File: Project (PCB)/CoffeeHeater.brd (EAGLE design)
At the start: 231.1 x 182.6 mm, 9 parts, among them U1 POCKETBEAGLE, U2 0.56_HEX_BACKPACK

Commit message: Updated the library with all the devices and made progress in the schematics and the board
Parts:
- removed D2, D3: LED, ENGI301:EIA-STD
- added BLUE, GREEN, RED: LED, ENGI301:EIA-STD
- added C1, C2: 10uF/16V X5R, microbuilder:0805-NO
- added C3: 0.1uF, microbuilder:0805-NO
- added C4: 10pF, microbuilder:0805-NO
- added C5, C6, C7: 22uF/10V X5R, microbuilder:0805-NO
- added C8: 1uF/10V X5R, microbuilder:0805-NO
- added L1: NRS5030T1R0NMGJ, microbuilder:INDUCTOR_5X5MM_TDK_VLC5045
- added Q1: BSS138, microbuilder:SOT23-WIDE
- added R10, R6, R9: 105K, microbuilder:0805-NO
- added R4: 2.2k, ENGI301:R0603
- added R5, R7: 1M, microbuilder:0805-NO
- added R8: 1K, microbuilder:0805-NO
- added U$2: TIP32C_TRANSISTOR, CoffeeHeater:TIP32C_TRANSISTOR
- added U$3: DIODE, CoffeeHeater:DIODE
- added U$4: HEATING_PAD, CoffeeHeater:HEATING_PAD
- added U3: TPS63060, microbuilder:PWSON-N10
- added X1: (no value), microbuilder:TERMBLOCK_1X2-3.5MM
- D1: value LED -> GREEN; device ENGI301:EIA-STD -> microbuilder:CHIPLED_0805_NOOUTLINE
- moved U$1 190.5 mm to (77.5, 78.7)
- moved D1 181.6 mm to (143.5, 85.1)
- moved R1 149.9 mm to (80.0, 40.6)
- moved R3 102.4 mm to (27.9, 52.1)
- moved R2 101.2 mm to (27.9, 45.7)
- moved U1 96.8 mm to (9.40, 58.7)
- moved U2 78.8 mm to (35.6, 24.1)
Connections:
- removed net VIN: U1.1
- new net 12V_VIN: C1.1, C2.1, R9.1, U$2.C, U3.2, X1.2
- new net 5.0V: C5.1, C6.1, C7.1, C8.1, D1.A, R5.2, R7.2, U1.1, U3.9
- new net BASE: U$2.B, U$3.OUT
- new net ENABLE: R9.2, U3.3
- new net HEAT_CONTROL: U$3.IN, U1.60
- new net N$1: U$2.E, U$4.GND
- new net N$10: D1.C, R8.1
- new net N$11: Q1.3, R8.2
- new net N$6: L1.P$1, U3.1
- new net N$7: L1.P$2, U3.10
- new net N$8: C3.1, U3.6
- new net N$9: C4.1, R5.1, R6.2, U3.8
- new net PG: Q1.1, R7.1, U3.5
- new net PS: R10.1, U3.4
- new net TEMP: R4.2, U$1.DQ, U1.69
- net GND: now also BLUE.P$2, C1.2, C2.2, C3.2, C4.2, C5.2, C6.2, C7.2, C8.2, GREEN.P$2, Q1.2, R10.2, R6.1, RED.P$2, U$1.GND, U$4.VDD, U3.7, U3.THERMAL@1, U3.THERMAL@10, U3.THERMAL@11, U3.THERMAL@12, U3.THERMAL@13, U3.THERMAL@14, U3.THERMAL@5, U3.THERMAL@6, U3.THERMAL@7, U3.THERMAL@8, U3.THERMAL@9, X1.1; no longer D1.P$2, D2.P$2, D3.P$2
- net N$3: now also U1.71; no longer U1.19
- net START_0: now also BLUE.P$1, U1.54; no longer D1.P$1, U1.55
- net START_1: now also GREEN.P$1, U1.56; no longer D2.P$1, U1.60
- net START_2: now also RED.P$1; no longer D3.P$1
- net VDD_5V: now also R4.1, U$1.VDD
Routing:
- added copper zone on layer 16, net GND
- added copper zone on layer 1, net VDD_3P3V
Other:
- board size 231.1 x 182.6 mm -> 152.4 x 101.6 mm
- board text added: "HEATING_PAD"
- board text added: "TIP32C_Potentiometer"

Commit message: Started routing some of the connections
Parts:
- moved R2 17.0 mm to (45.0, 45.5)
- moved R3 17.0 mm to (45.0, 51.8)
- moved R4 0.25 mm to (70.1, 87.6), turned to 180 degrees
- flipped BLUE to the bottom
- flipped GREEN to the bottom
- flipped R1 to the bottom
- flipped RED to the bottom
- flipped U2 to the bottom
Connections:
- net GND: now also U$4.GND; no longer U$4.VDD
- net N$1: now also U$4.VDD; no longer U$4.GND
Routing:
- net START_0: track 0.00 -> 104.9 mm
- net VDD_5V: track 0.00 -> 98.5 mm
- net HEAT_CONTROL: track 0.00 -> 96.7 mm
- net START_1: track 0.00 -> 92.6 mm
- net START_2: track 0.00 -> 81.9 mm
- net N$2: track 0.00 -> 75.1 mm
- net N$3: track 0.00 -> 63.6 mm
- net TEMP: track 0.00 -> 41.5 mm
- net I2C_SDA: track 0.00 -> 33.2 mm
- net I2C_SCL: track 0.00 -> 33.0 mm
- net N$1: track 0.00 -> 20.8 mm
- net BASE: track 0.00 -> 12.7 mm

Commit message: Connect all the GND nets
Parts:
- moved R8 0.80 mm to (143.5, 73.7), turned to 270 degrees
- moved D1 0.25 mm to (143.5, 84.8), turned to 180 degrees
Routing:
- net GND: track 0.00 -> 53.5 mm, vias 0 -> 18
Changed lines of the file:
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@@
 <attribute name="NAME" x="134.747" y="83.312" size="0.8128" layer="25" ratio="18" rot="R90"/>
 </element>
-<element name="D1" library="microbuilder" package="CHIPLED_0805_NOOUTLINE" value="GREEN" x="143.51" y="85.09">
-<attribute name="NAME" x="142.494" y="83.312" size="0.8128" layer="25" ratio="18" rot="R90"/>
-<attribute name="VALUE" x="144.907" y="83.566" size="0.4064" layer="27" ratio="10" rot="R90"/>
-</element>
-<element name="R8" library="microbuilder" package="0805-NO" value="1K" x="143.764" y="72.898" rot="R90">
-<attribute name="NAME" x="142.621" y="71.12" size="0.8128" layer="25" ratio="18" rot="R90"/>
+<element name="D1" library="microbuilder" package="CHIPLED_0805_NOOUTLINE" value="GREEN" x="143.51" y="84.836" rot="R180">
+<attribute name="NAME" x="141.478" y="84.328" size="0.8128" layer="25" ratio="18" rot="R270"/>
+<attribute name="VALUE" x="144.907" y="84.836" size="0.4064" layer="27" ratio="10" rot="R270"/>
+</element>
+<element name="R8" library="microbuilder" package="0805-NO" value="1K" x="143.51" y="73.66" rot="R270">
+<attribute name="NAME" x="144.653" y="75.438" size="0.8128" layer="25" ratio="18" rot="R270"/>
 </element>
 <element name="X1" library="microbuilder" package="TERMBLOCK_1X2-3.5MM" value="" x="86.106" y="66.167" rot="R90">
@@
 </polygon>
 <contactref element="U$4" pad="GND"/>
-<wire x1="129.54" y1="86.04" x2="135.89" y2="86.04" width="0" layer="19" extent="1-1"/>
-<wire x1="123.19" y1="86.04" x2="129.54" y2="86.04" width="0" layer="19" extent="1-1"/>
-<wire x1="116.84" y1="86.04" x2="123.19" y2="86.04" width="0" layer="19" extent="1-1"/>
-<wire x1="130.318" y1="72.71" x2="129.54" y2="86.04" width="0" layer="19" extent="1-1"/>
-<wire x1="137.348" y1="64.008" x2="130.318" y2="72.71" width="0" layer="19" extent="1-1"/>
-<wire x1="132.334" y1="54.676" x2="137.348" y2="64.008" width="0" layer="19" extent="1-1"/>
-<wire x1="123.444" y1="56.576" x2="132.334" y2="54.676" width="0" layer="19" extent="1-1"/>
-<wire x1="117.79" y1="50.292" x2="123.444" y2="56.576" width="0" layer="19" extent="1-1"/>
-<wire x1="112.966" y1="67.218" x2="123.444" y2="56.576" width="0" layer="19" extent="1-1"/>
-<wire x1="112.966" y1="67.618" x2="112.966" y2="67.218" width="0" layer="19" extent="1-1"/>
-<wire x1="112.966" y1="68.018" x2="112.966" y2="67.618" width="0" layer="19" extent="1-1"/>
-<wire x1="112.966" y1="68.418" x2="112.966" y2="68.018" width="0" layer="19" extent="1-1"/>
-<wire x1="112.106" y1="67.818" x2="112.966" y2="67.618" width="0" layer="19" extent="1-1"/>
-<wire x1="111.506" y1="67.818" x2="112.106" y2="67.818" width="0" layer="19" extent="1-1"/>
-<wire x1="110.906" y1="67.818" x2="111.506" y2="67.818" width="0" layer="19" extent="1-1"/>
+<via x="34.036" y="40.386" extent="1-16" drill="0.35"/>
+<wire x1="34.036" y1="35.56" x2="34.036" y2="40.386" width="0.1524" layer="1"/>
+<via x="116.84" y="88.646" extent="1-16" drill="0.35"/>
+<via x="123.19" y="88.646" extent="1-16" drill="0.35"/>
+<via x="129.54" y="88.646" extent="1-16" drill="0.35"/>
+<via x="135.89" y="88.646" extent="1-16" drill="0.35"/>
+<wire x1="116.84" y1="86.04" x2="116.84" y2="88.646" width="0.1524" layer="1"/>
+<wire x1="123.19" y1="86.04" x2="123.19" y2="88.646" width="0.1524" layer="1"/>
+<wire x1="129.54" y1="86.04" x2="129.54" y2="88.646" width="0.1524" layer="1"/>
+<wire x1="135.89" y1="86.04" x2="135.89" y2="88.646" width="0.1524" layer="1"/>
+<via x="140.97" y="64.008" extent="1-16" drill="0.35"/>
+<via x="127.762" y="72.644" extent="1-16" drill="0.35"/>
+<via x="123.444" y="58.42" extent="1-16" drill="0.35"/>
+<via x="132.334" y="52.578" extent="1-16" drill="0.35"/>
+<via x="120.904" y="50.292" extent="1-16" drill="0.35"/>
+<wire x1="130.318" y1="72.71" x2="130.252" y2="72.644" width="0.1524" layer="1"/>
+<wire x1="130.252" y1="72.644" x2="127.762" y2="72.644" width="0.1524" layer="1"/>
+<wire x1="137.348" y1="64.008" x2="140.97" y2="64.008" width="0.1524" layer="1"/>
+<wire x1="132.334" y1="54.676" x2="132.334" y2="52.578" width="0.1524" layer="1"/>
+<wire x1="123.444" y1="56.576" x2="123.444" y2="58.42" width="0.1524" layer="1"/>
+<wire x1="117.79" y1="50.292" x2="120.904" y2="50.292" width="0.1524" layer="1"/>
+<via x="115.824" y="13.716" extent="1-16" drill="0.35"/>
+<wire x1="121.92" y1="13.97" x2="120.396" y2="13.97" width="0.1524" layer="1"/>
+<wire x1="120.396" y1="13.97" x2="119.888" y2="13.462" width="0.1524" layer="1"/>
+<wire x1="119.888" y1="13.462" x2="116.078" y2="13.462" width="0.1524" layer="1"/>
+<wire x1="116.078" y1="13.462" x2="115.824" y2="13.716" width="0.1524" layer="1"/>
+<via x="71.628" y="12.7" extent="1-16" drill="0.35"/>
+<via x="72.136" y="22.86" extent="1-16" drill="0.35"/>
+<via x="72.136" y="30.48" extent="1-16" drill="0.35"/>
+<wire x1="74.18" y1="30.48" x2="72.136" y2="30.48" width="0.1524" layer="16"/>
+<wire x1="74.18" y1="22.86" x2="72.136" y2="22.86" width="0.1524" layer="16"/>
+<wire x1="74.18" y1="12.7" x2="71.628" y2="12.7" width="0.1524" layer="16"/>
+<via x="94.234" y="53.086" extent="1-16" drill="0.35"/>
+<via x="100.584" y="53.086" extent="1-16" drill="0.35"/>
+<via x="86.106" y="72.39" extent="1-16" drill="0.35"/>
+<wire x1="94.234" y1="55.438" x2="94.234" y2="53.086" width="0.1524" layer="1"/>
+<wire x1="100.584" y1="55.438" x2="100.584" y2="53.086" width="0.1524" layer="1"/>
+<wire x1="86.106" y1="67.967" x2="86.106" y2="72.39" width="0.1524" layer="1"/>
+<via x="74.93" y="81.534" extent="1-16" drill="0.35"/>
+<wire x1="74.93" y1="78.74" x2="74.93" y2="81.534" width="0.1524" layer="1"/>
+<wire x1="112.966" y1="68.418" x2="112.006" y2="69.293" width="0" layer="19" extent="1-1"/>
+<wire x1="112.966" y1="68.018" x2="112.966" y2="68.418" width="0" layer="19" extent="1-1"/>
+<wire x1="112.966" y1="67.618" x2="112.966" y2="68.018" width="0" layer="19" extent="1-1"/>
+<wire x1="112.966" y1="67.218" x2="112.966" y2="67.618" width="0" layer="19" extent="1-1"/>
+<wire x1="112.106" y1="67.818" x2="112.966" y2="68.018" width="0" layer="19" extent="1-1"/>
+<wire x1="111.506" y1="67.818" x2="110.906" y2="67.818" width="0" layer="19" extent="1-1"/>
 <wire x1="110.046" y1="67.618" x2="110.906" y2="67.818" width="0" layer="19" extent="1-1"/>
 <wire x1="110.046" y1="67.218" x2="110.046" y2="67.618" width="0" layer="19" extent="1-1"/>
 <wire x1="110.046" y1="68.018" x2="110.046" y2="67.618" width="0" layer="19" extent="1-1"/>
 <wire x1="110.046" y1="68.418" x2="110.046" y2="68.018" width="0" layer="19" extent="1-1"/>
-<wire x1="112.006" y1="69.293" x2="112.966" y2="68.418" width="0" layer="19" extent="1-1"/>
-<wire x1="100.584" y1="55.438" x2="110.046" y2="67.218" width="0" layer="19" extent="1-1"/>
-<wire x1="94.234" y1="55.438" x2="100.584" y2="55.438" width="0" layer="19" extent="1-1"/>
-<wire x1="86.106" y1="67.967" x2="94.234" y2="55.438" width="0" layer="19" extent="1-1"/>
-<wire x1="74.93" y1="78.74" x2="86.106" y2="67.967" width="0" layer="19" extent="1-1"/>
-<wire x1="77.51" y1="40.64" x2="94.234" y2="55.438" width="0" layer="19" extent="1-1"/>
-<wire x1="74.18" y1="30.48" x2="77.51" y2="40.64" width="0" layer="19" extent="16-16"/>
-<wire x1="74.18" y1="22.86" x2="74.18" y2="30.48" width="0" layer="19" extent="16-16"/>
-<wire x1="74.18" y1="12.7" x2="74.18" y2="22.86" width="0" layer="19" extent="16-16"/>
-<wire x1="40.708" y1="87.604" x2="74.93" y2="78.74" width="0" layer="19" extent="1-1"/>
-<wire x1="33.088" y1="87.604" x2="40.708" y2="87.604" width="0" layer="19" extent="1-1"/>
-<wire x1="40.708" y1="64.744" x2="40.708" y2="87.604" width="0" layer="19" extent="1-1"/>
-<wire x1="33.088" y1="64.744" x2="40.708" y2="64.744" width="0" layer="19" extent="1-1"/>
-<wire x1="33.088" y1="62.204" x2="33.088" y2="64.744" width="0" layer="19" extent="1-1"/>
-<wire x1="34.036" y1="35.56" x2="33.088" y2="62.204" width="0" layer="19" extent="1-1"/>
-<wire x1="121.92" y1="13.97" x2="117.79" y2="50.292" width="0" layer="19" extent="1-1"/>
 </signal>
 <signal name="I2C_SDA">
@@
 <contactref element="C8" pad="1"/>
 <contactref element="U1" pad="1"/>
-<wire x1="135.89" y1="84.14" x2="143.51" y2="84.04" width="0" layer="19" extent="1-1"/>
+<wire x1="135.89" y1="84.14" x2="143.51" y2="85.886" width="0" layer="19" extent="1-1"/>
 <wire x1="129.54" y1="84.14" x2="135.89" y2="84.14" width="0" layer="19" extent="1-1"/>
 <wire x1="123.19" y1="84.14" x2="129.54" y2="84.14" width="0" layer="19" extent="1-1"/>
@@
 <contactref element="D1" pad="C"/>
 <contactref element="R8" pad="1"/>
-<wire x1="143.764" y1="71.948" x2="143.51" y2="86.14" width="0" layer="19" extent="1-1"/>
+<wire x1="143.51" y1="74.61" x2="143.51" y2="83.786" width="0" layer="19" extent="1-1"/>
 </signal>
 <signal name="N$11">
 <contactref element="R8" pad="2"/>
 <contactref element="Q1" pad="3"/>
-<wire x1="132.318" y1="73.66" x2="143.764" y2="73.848" width="0" layer="19" extent="1-1"/>
+<wire x1="132.318" y1="73.66" x2="143.51" y2="72.71" width="0" layer="19" extent="1-1"/>
 </signal>
 <signal name="ENABLE">

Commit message: Added all of the connections
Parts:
- moved R5 30.1 mm to (116.6, 73.7), turned to 270 degrees
- moved R6 26.4 mm to (113.0, 73.7), turned to 270 degrees
- moved C4 25.0 mm to (116.8, 79.5)
- moved C3 12.8 mm to (116.8, 66.5)
- moved R7 8.16 mm to (123.1, 66.3), turned to 180 degrees
- moved Q1 4.44 mm to (135.6, 72.6)
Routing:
- net 5.0V: track 0.00 -> 234.1 mm
- net PG: track 0.00 -> 30.2 mm
- net N$6: track 0.00 -> 29.2 mm
- net N$7: track 0.00 -> 22.6 mm
- net PS: track 0.00 -> 18.9 mm
- net N$9: track 0.00 -> 14.0 mm
- net ENABLE: track 0.00 -> 13.3 mm
- net N$10: track 0.00 -> 9.18 mm
- net N$8: track 0.00 -> 6.91 mm
- net N$11: track 0.00 -> 6.90 mm
- added copper zone on layer 1, net 12V_VIN

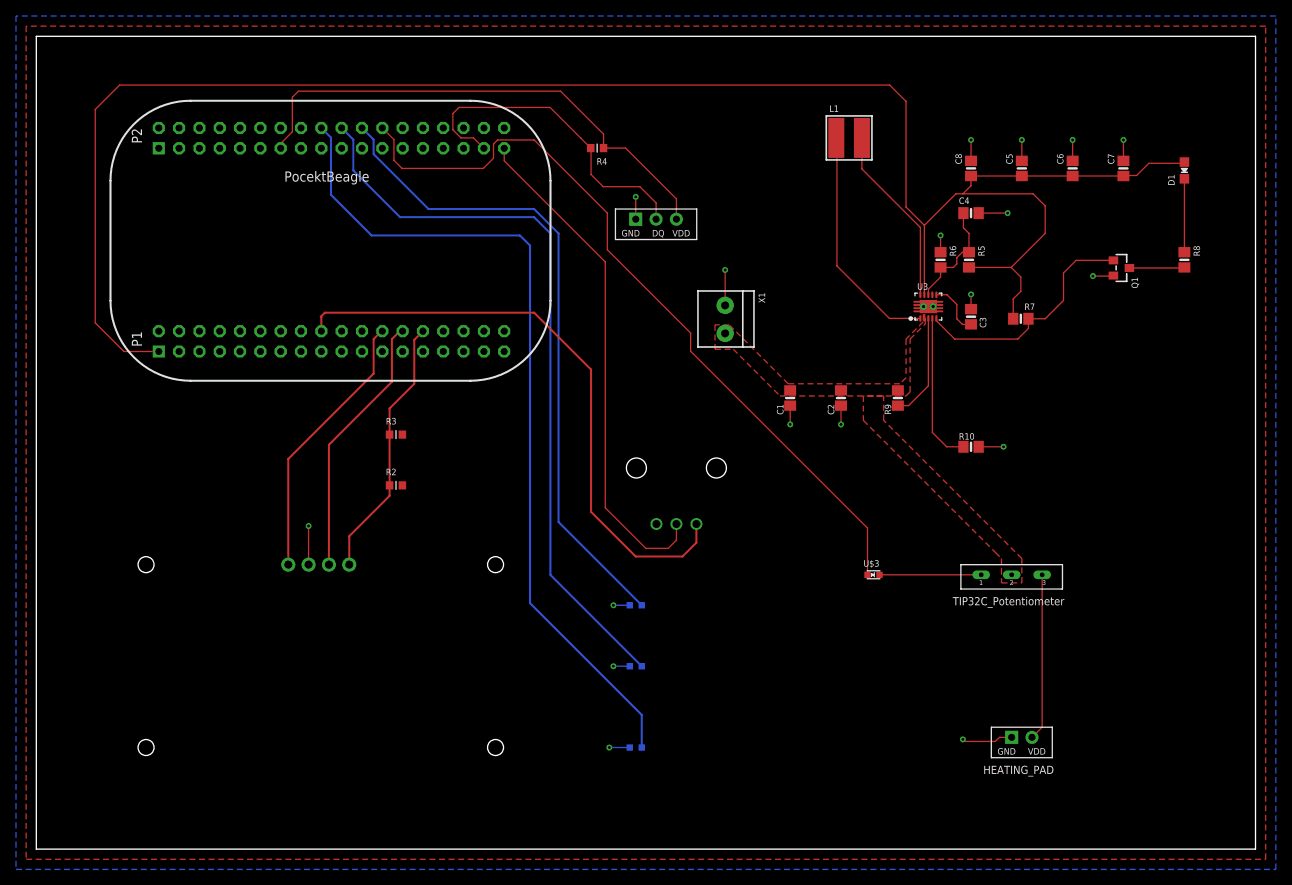
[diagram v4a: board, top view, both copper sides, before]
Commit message: Added mechanical parts and updated routes.
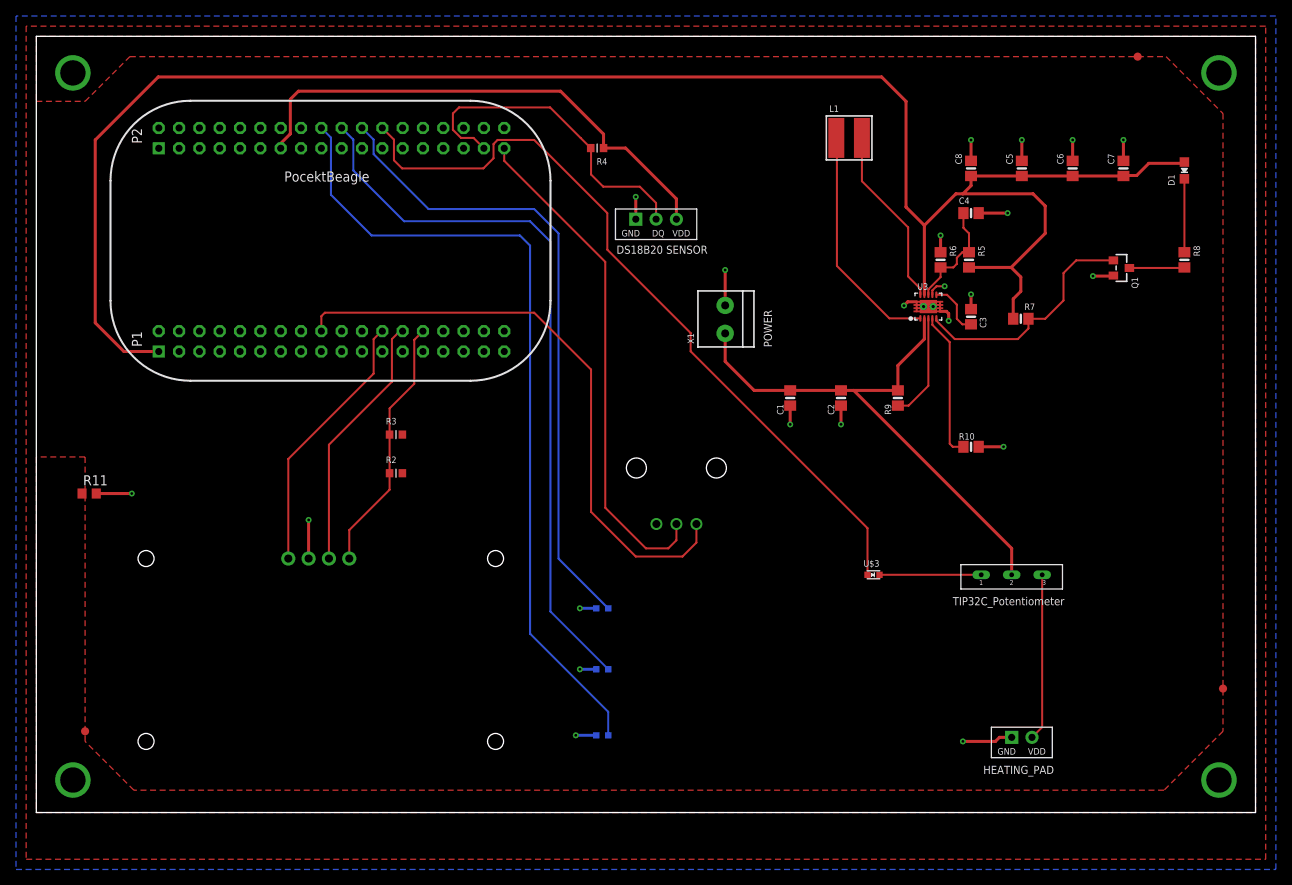
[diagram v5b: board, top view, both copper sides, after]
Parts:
- added FUD1, FUD2, FUD3: FIDUCIAL, Whac-a-mole:FIDUCIAL_40MIL
- added MGT1, MGT2, MGT3, MGT4: MOUNTING_HOLE, Whac-a-mole:MOUNTING_HOLE
- added R11: 0.1 Ohm, Whac-a-mole:R0805
- moved BLUE 4.46 mm to (70.7, 14.2)
- moved GREEN 4.21 mm to (70.7, 22.5)
- moved RED 4.21 mm to (70.7, 30.1)
- moved R2 1.52 mm to (45.0, 47.0)
- moved U2 0.76 mm to (35.6, 24.9)
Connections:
- new net CGND: MGT1.P$1, MGT2.P$1, MGT3.P$1, MGT4.P$1, R11.1
- net GND: now also R11.2
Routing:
- net 12V_VIN: track 0.00 -> 68.2 mm
- net GND: track 53.5 -> 66.4 mm, vias 18 -> 22
- net START_0: track 104.9 -> 101.6 mm
- net START_1: track 92.6 -> 90.7 mm
- net 5.0V: track 234.1 -> 232.7 mm
- net START_2: track 81.9 -> 80.5 mm
- net VDD_5V: track 98.5 -> 97.8 mm
- net I2C_SDA: track 33.2 -> 32.4 mm
- net I2C_SCL: track 33.0 -> 32.2 mm
- added copper zone on layer 1, net CGND
- removed copper zone on layer 1, net 12V_VIN
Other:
- board size 152.4 x 101.6 mm -> 152.4 x 97 mm
- board text added: "DS18B20 SENSOR"
- board text added: "POWER"
